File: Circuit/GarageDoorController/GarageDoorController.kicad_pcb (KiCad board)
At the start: 2 copper layers, 71.5 x 50.6 mm, 27 parts, among them J3 JST PH 2-pin, J4 JST PH 4-pin, U1 XIAO-ESP32-C3-DIP, U3 TLP222A, U4 PC817, U5 R-78E5.0-0.5

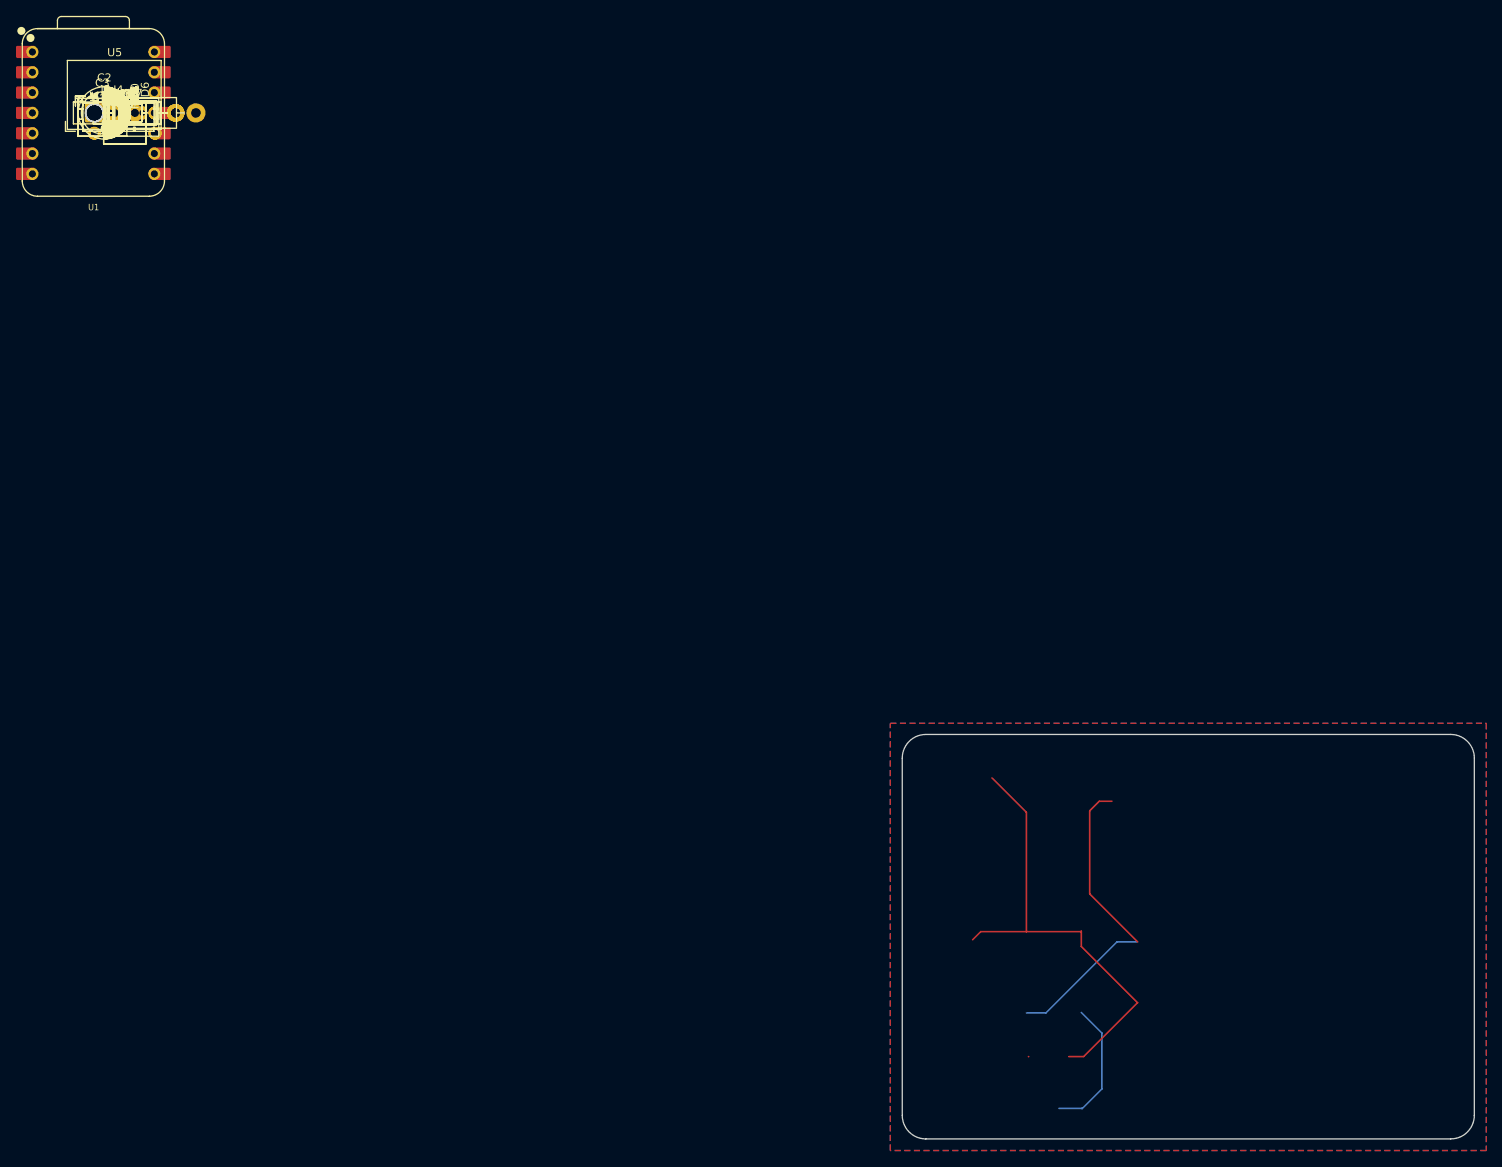
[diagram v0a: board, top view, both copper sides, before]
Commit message: Rev 1 PCB: routed board and fab files
- 2-layer, 71.5 x 50.6 mm, rounded corners, four M2 mounting holes,
  GND pours both layers
- Opener parts placed and routed: 24 V input chain (J4, F1, D5, D8,
  C2/D6, U5 R-78E, C3/D7 to XIAO 5 V), U3 TLP222A on PB, U4 PC817 on FLASH
- Power path 0.5 mm; direct F.Cu ground returns U5 to C2/C3
- DRC: 0 errors, 0 unconnected, 19 cosmetic warnings (DRC.rpt)
- Gerbers and drill files in gerbers/, zipped for the fab
- Ignore .DS_Store

Co-Authored-By: Claude Opus 5.5 <noreply@anthropic.com>
Claude-Session: https://claude.ai/code/session_01BUyReJ4iEoMZE9spF9mEyw
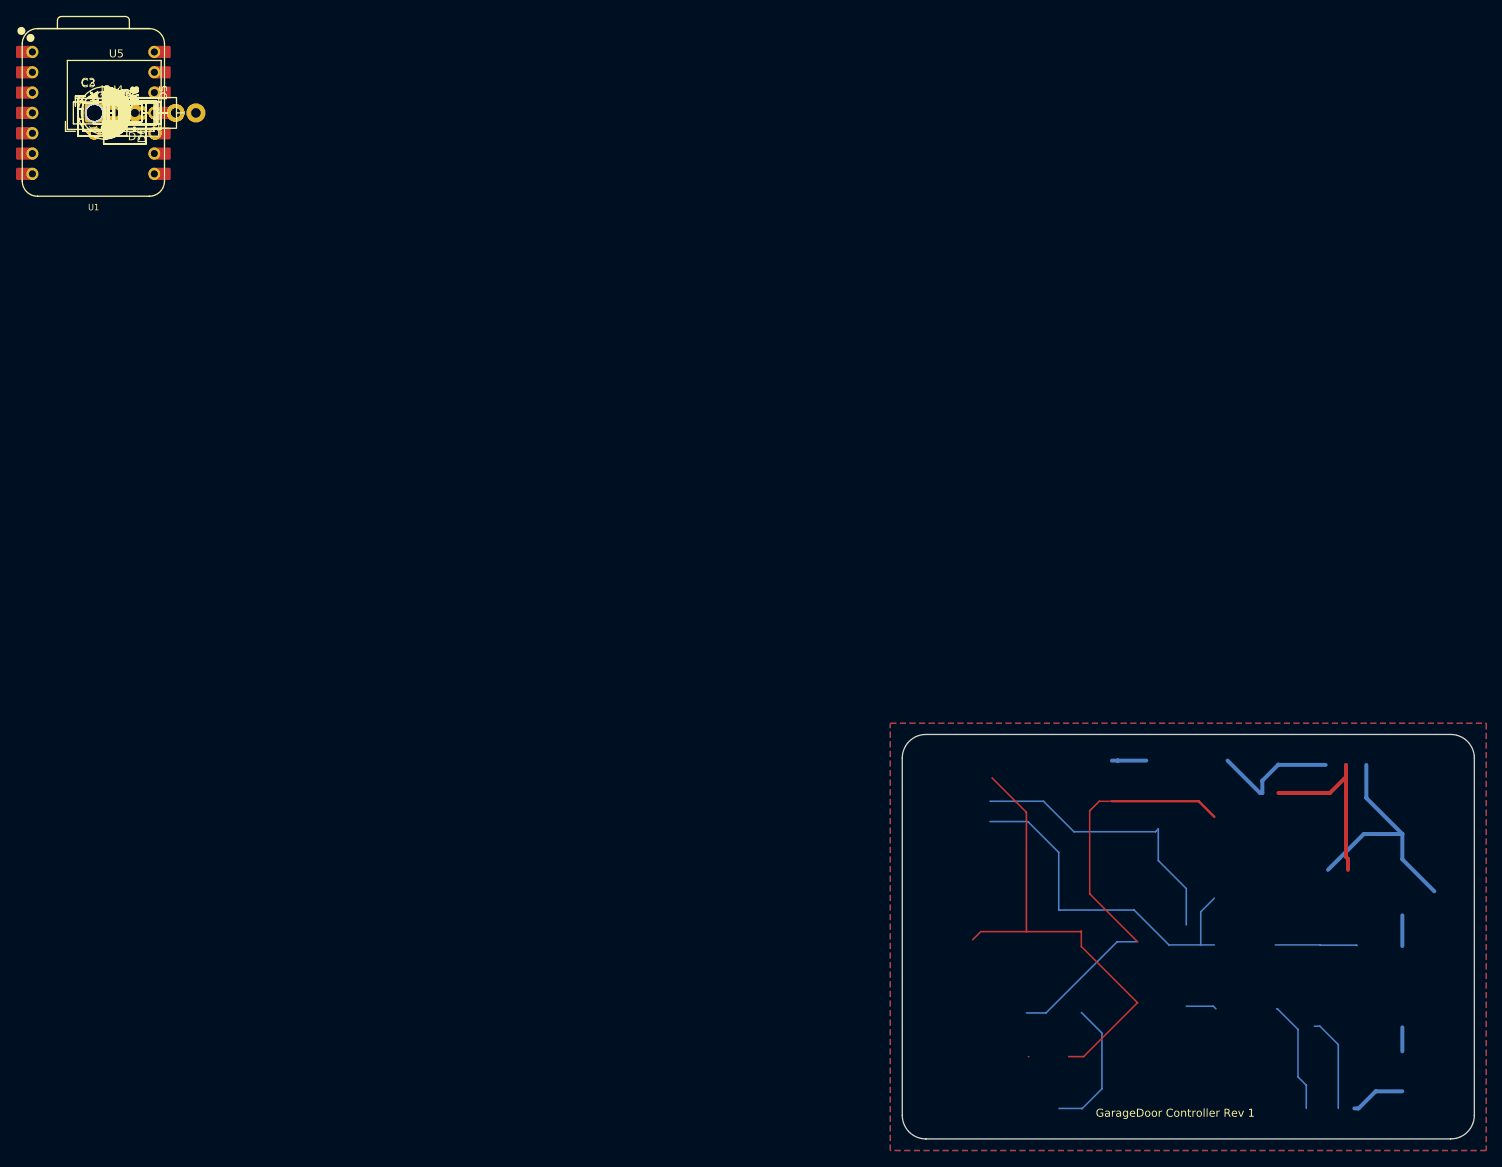
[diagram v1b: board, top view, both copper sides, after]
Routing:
- net OPENER_MOVING: track 0.00 -> 45.2 mm
- net OPENER_TRIG: track 0.00 -> 36.2 mm
- net Net-(D6-A2): track 0.00 -> 30.5 mm
- net GND: track 0.04 -> 22.6 mm
- net Net-(D7-A): track 0.00 -> 16.3 mm
- net /Opener control/PB: track 0.00 -> 14.0 mm
- net +3V3: track 39.7 -> 53.3 mm
- net /Opener control/FLASH: track 0.00 -> 11.9 mm
- net Net-(D4-K): track 0.00 -> 10.3 mm
- net /Opener control/OPENER_24V: track 0.00 -> 6.89 mm
- net XIAO_5V: track 0.00 -> 4.30 mm
- net Net-(D5-K): track 0.00 -> 3.84 mm
- net Net-(R7-Pad2): track 0.00 -> 3.83 mm
- net Net-(D5-A): track 0.00 -> 3.00 mm
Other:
- board text added: "GarageDoor Controller Rev 1"
